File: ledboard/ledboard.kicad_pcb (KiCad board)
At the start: 2 copper layers, 100 x 80 mm, 88 parts, among them J1 Barrel_Jack_Switch, J2 Conn_02x20_Odd_Even, J3 Conn_01x02, U1 TPS54332DDA, U2 TPS7A5301BRPSR, U3 TPS2121, U4 TBD62083AFG, U5 TBD62783AFG, U6 TBD62083AFG, U7 TBD62083AFG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

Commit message: PCBデザイン. 未結線がなくなったところまで.
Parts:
- moved C2 64.6 mm to (166.2, 73.2), turned to 90 degrees
- moved R12 57.7 mm to (170.7, 115.9), turned to -90 degrees
- moved R13 56.9 mm to (173.7, 116.8)
- moved R1 56.4 mm to (165.2, 59.3), turned to 180 degrees
- moved R10 56.2 mm to (168.3, 114.6), turned to -90 degrees
- moved R16 54.6 mm to (159.6, 117.6)
- moved C12 54.6 mm to (167.8, 105.8), turned to 0 degrees
- moved U3 54.3 mm to (163.6, 119.3)
- moved R15 54.2 mm to (168.2, 124.6), turned to 90 degrees
- moved J3 53.9 mm to (171.4, 112.3)
- moved C13 53.5 mm to (167.3, 108.2), turned to 0 degrees
- moved C14 53.5 mm to (167.3, 110.1), turned to 0 degrees
- moved C18 52.9 mm to (160.2, 120.6)
- moved U2 52.5 mm to (160.9, 99.6)
- moved C4 52.2 mm to (162.6, 62.0)
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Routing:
- net /LED_and_Conn/IO1_P: track 0.00 -> 127.1 mm, vias 0 -> 2
- net /LED_and_Conn/IO2_P: track 0.00 -> 122.8 mm, vias 0 -> 2
- net /LED_and_Conn/+5V_VCC: track 0.00 -> 122.2 mm
- net /LED_and_Conn/IO3_P: track 0.00 -> 118.0 mm, vias 0 -> 2
- net /LED_and_Conn/IO4_P: track 0.00 -> 113.6 mm, vias 0 -> 2
- net /LED_and_Conn/IO5_P: track 0.00 -> 109.5 mm, vias 0 -> 2
- net /LED_and_Conn/IO6_P: track 0.00 -> 106.6 mm, vias 0 -> 2
- net /LED_and_Conn/IO7_P: track 0.00 -> 103.3 mm, vias 0 -> 2
- net /LED_and_Conn/IO8_P: track 0.00 -> 99.4 mm, vias 0 -> 2
- net /LED_and_Conn/IO9_P: track 0.00 -> 94.5 mm, vias 0 -> 1
- net /LED_and_Conn/IO10_P: track 0.00 -> 91.7 mm, vias 0 -> 1
- net /LED_and_Conn/IO12_P: track 0.00 -> 89.2 mm, vias 0 -> 1
- net /LED_and_Conn/IO11_P: track 0.00 -> 89.1 mm, vias 0 -> 1
- net /LED_and_Conn/IO13_P: track 0.00 -> 86.8 mm, vias 0 -> 1
- net /LED_and_Conn/IO14_P: track 0.00 -> 83.9 mm, vias 0 -> 1
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- added copper zone on F.Cu, net /+5V
- added copper zone on F.Cu, net /+5V_LOCAL
- added copper zone on F.Cu, net /LED_and_Conn/+5V_VCC
- added copper zone on B.Cu, net GND
- added copper zone on F.Cu, net GND
- added copper zone on F.Cu, net Net-(D1-K)
- added copper zone on F.Cu, net Net-(U2-BIAS)

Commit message: アートワーク完了.
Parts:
- moved C2 0.45 mm to (166.2, 72.8)
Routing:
- net GND: track 26.4 -> 25.7 mm, vias 77 -> 150
- net Net-(U1-COMP): track 7.92 -> 8.47 mm
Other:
- board text added: "*"
- board text added: "R32"
- board text added: "R33"
- board text added: "R34"
- board text added: "R35"
- board text added: "R36"
- board text added: "R37"
- board text added: "R38"
- board text added: "R39"
- board text added: "R40"

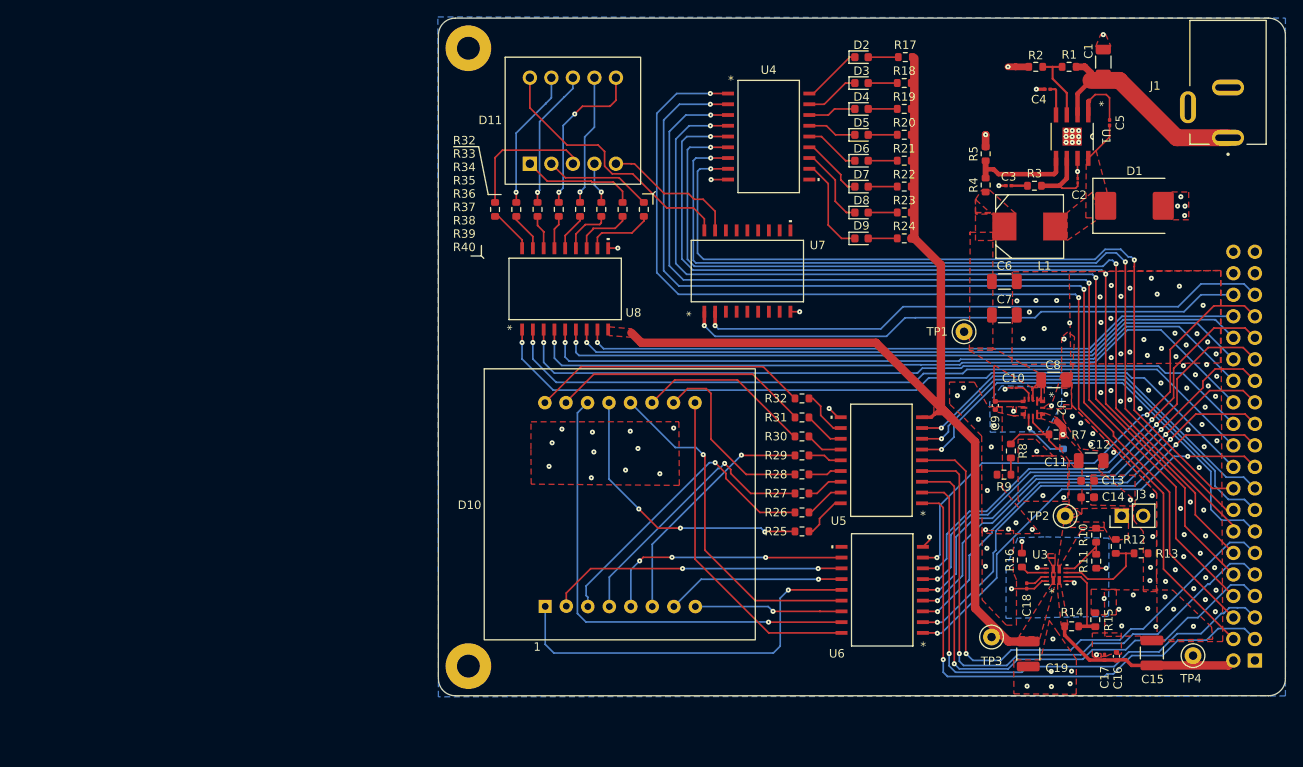
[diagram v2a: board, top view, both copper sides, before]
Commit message: LOGとボード名を追加します.
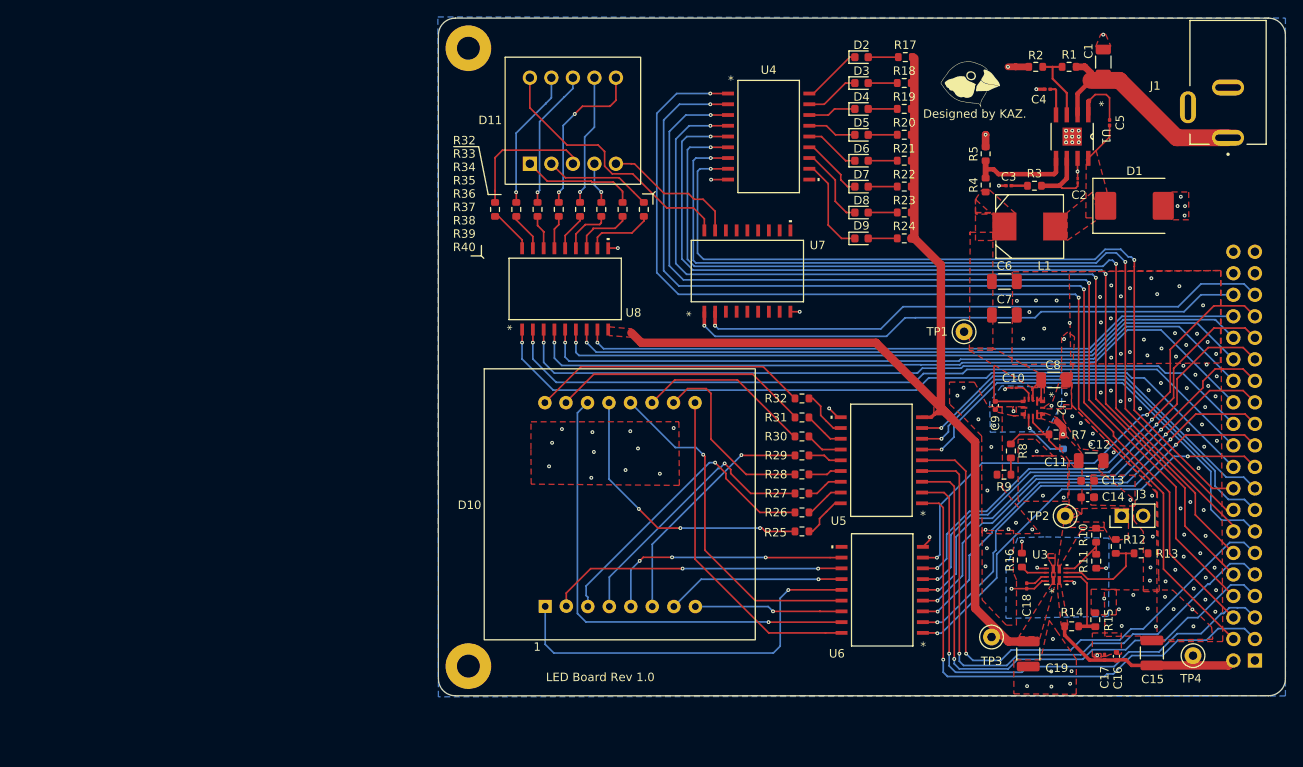
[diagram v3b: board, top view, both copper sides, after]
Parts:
- added G***: LOGO, MyLib:mylog, F.Cu at (153.4, 61.2)
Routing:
- net GND: vias 150 -> 151
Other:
- board text added: "LED Board Rev 1.0"

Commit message: 部品変更とアートワークの修正.
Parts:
- C10, C2: footprint Capacitor_SMD:C_01005_0402Metric -> Capacitor_SMD:C_0402_1005Metric
- J2: value Conn_02x20_Odd_Even -> DS1023-2*20SF11

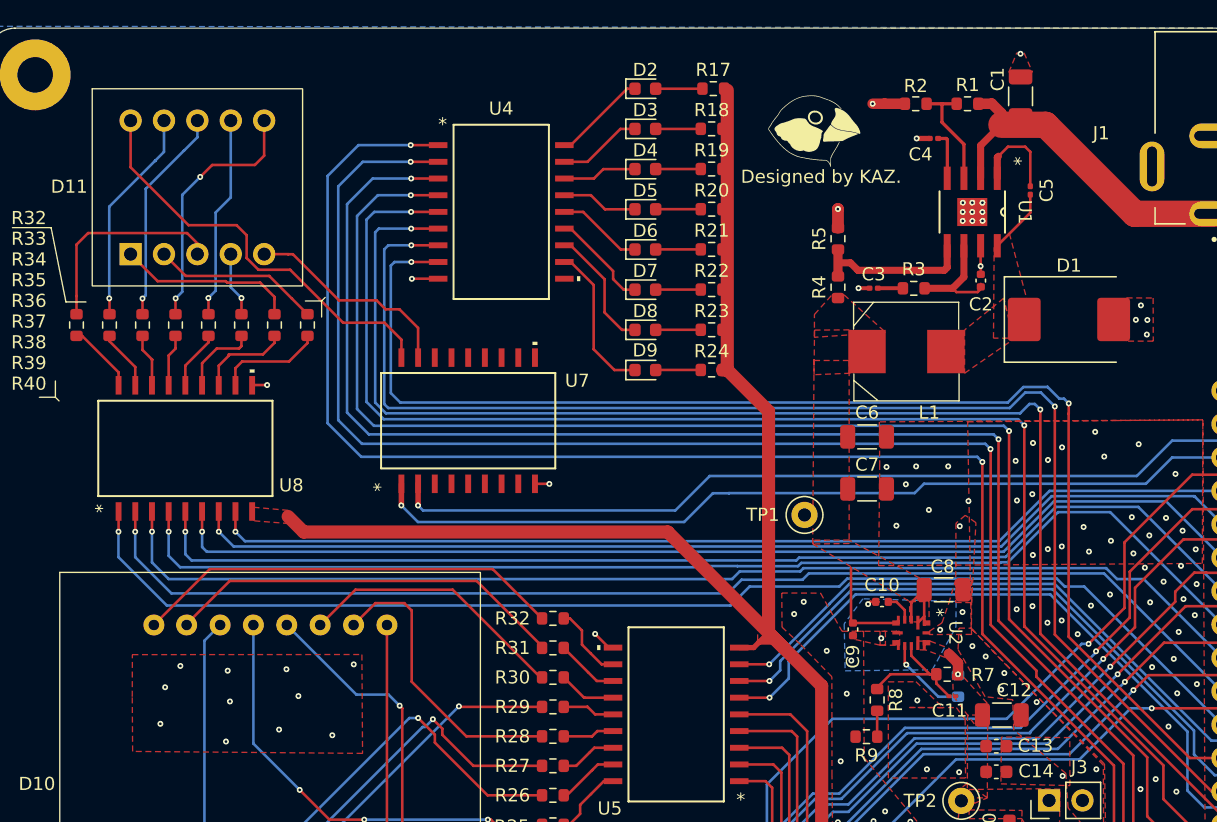
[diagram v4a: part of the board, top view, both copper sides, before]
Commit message: LSCS品番を追加. コンデンサの品番を変更します.
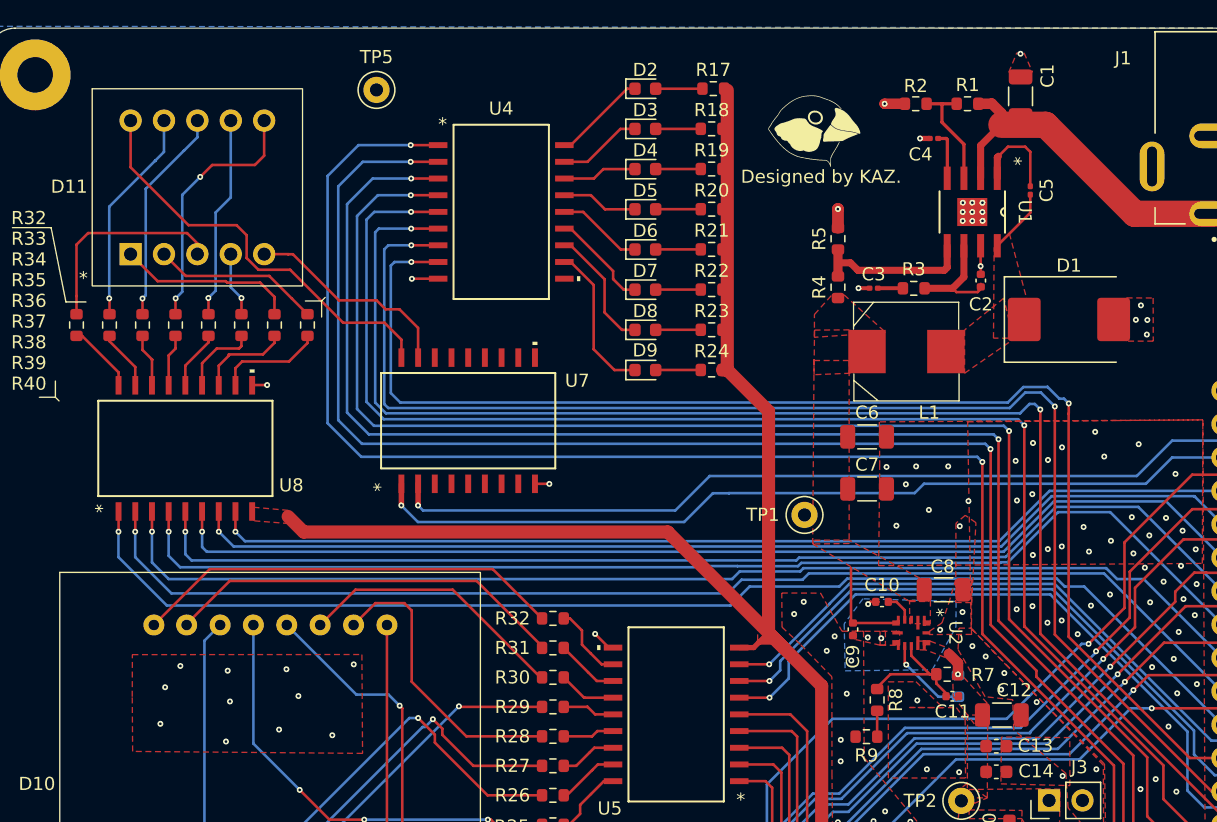
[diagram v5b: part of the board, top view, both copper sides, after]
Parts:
- added TP5: TestPoint, TestPoint:TestPoint_Keystone_5000-5004_Miniature, F.Cu at (120.2, 58.3)
- C11: footprint Capacitor_SMD:C_01005_0402Metric -> Capacitor_SMD:C_0402_1005Metric
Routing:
- net Net-(U2-BIAS): track 12.9 -> 7.52 mm
- net GND: track 25.7 -> 24.6 mm, vias 151 -> 154

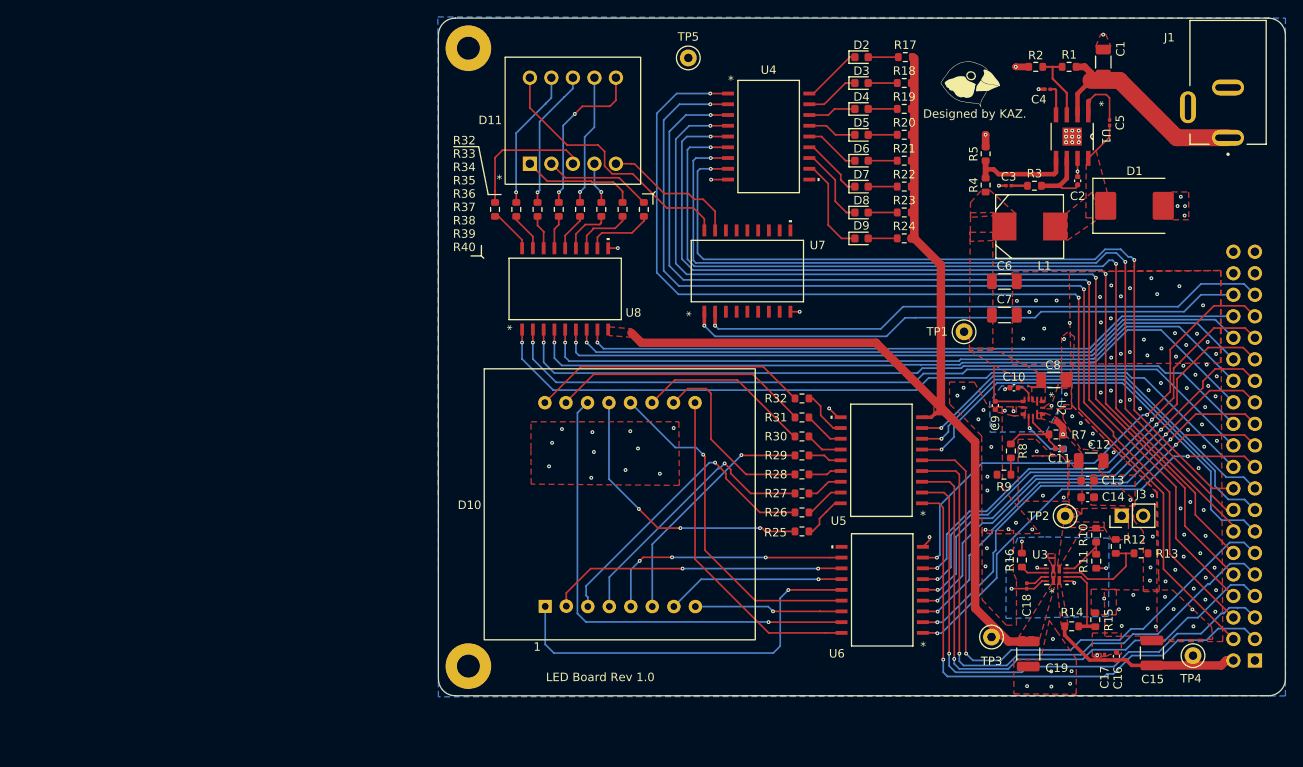
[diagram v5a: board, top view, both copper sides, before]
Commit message: L1をBOURNS SR8040-3R3Yに変更しました.
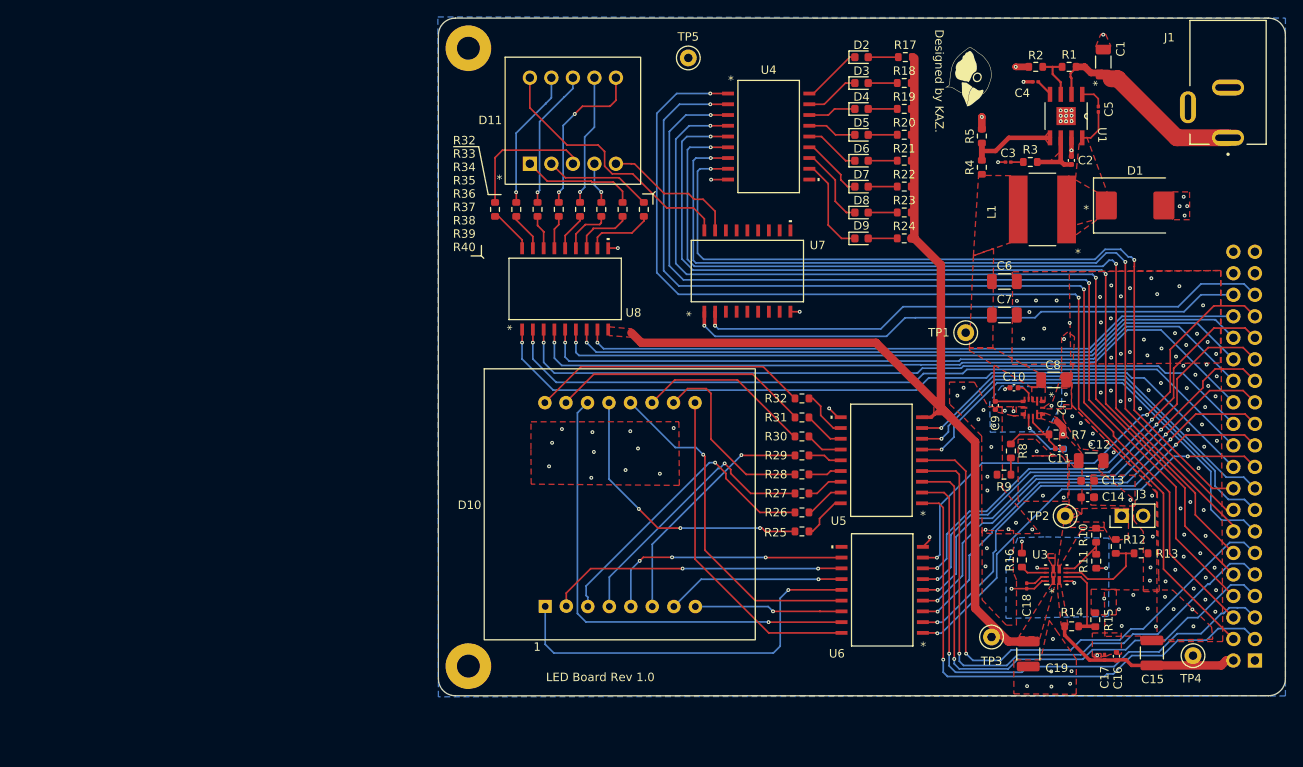
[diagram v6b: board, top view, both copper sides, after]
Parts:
- L1: footprint MyLib:SPM7054VC-3R3M-D -> MyLib:IND_BOURNS_SRN8040
- moved R3 2.85 mm to (160.6, 70.6)
- moved C3 2.78 mm to (158.0, 70.6)
- moved U1 2.53 mm to (164.8, 65.1)
- moved C2 2.52 mm to (165.4, 70.4)
- moved L1 2.51 mm to (162.0, 76.2)
- moved R4 2.14 mm to (154.9, 71.2)
- moved R5 2.14 mm to (154.9, 67.5)
- moved C5 2.07 mm to (168.6, 64.3)
- moved C4 1.66 mm to (161.2, 61.1)
- moved G*** 0.78 mm to (153.5, 60.4), turned to -90 degrees
- moved TP1 0.22 mm to (152.9, 90.7)
- moved D1 0.09 mm to (172.9, 75.7)
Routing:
- net Net-(U1-BOOT): track 7.21 -> 3.03 mm
- net Net-(U1-VIN): track 26.7 -> 23.8 mm
- net Net-(U1-EN): track 8.65 -> 5.93 mm
- net Net-(U1-SS): track 3.68 -> 2.05 mm
- net Net-(U1-VSENSE): track 12.3 -> 10.7 mm
- net Net-(U1-COMP): track 8.47 -> 6.95 mm
- added copper zone on F.Cu, net Net-(U1-COMP)
- added copper zone on F.Cu, net Net-(U1-VSENSE)
